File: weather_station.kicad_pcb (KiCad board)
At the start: 2 copper layers, 28 parts, among them J1 Conn_01x10_Pin, J2 Conn_01x04, J3 Conn_01x04, J5 USB_C_Receptacle_USB2.0_16P, J6 JTAG_connector, SW1 SW_Push, U1 USBLC6-2SC6, U2 AZ1117CH2-3.3, U4 STM32F103RGTx, X1 831066657

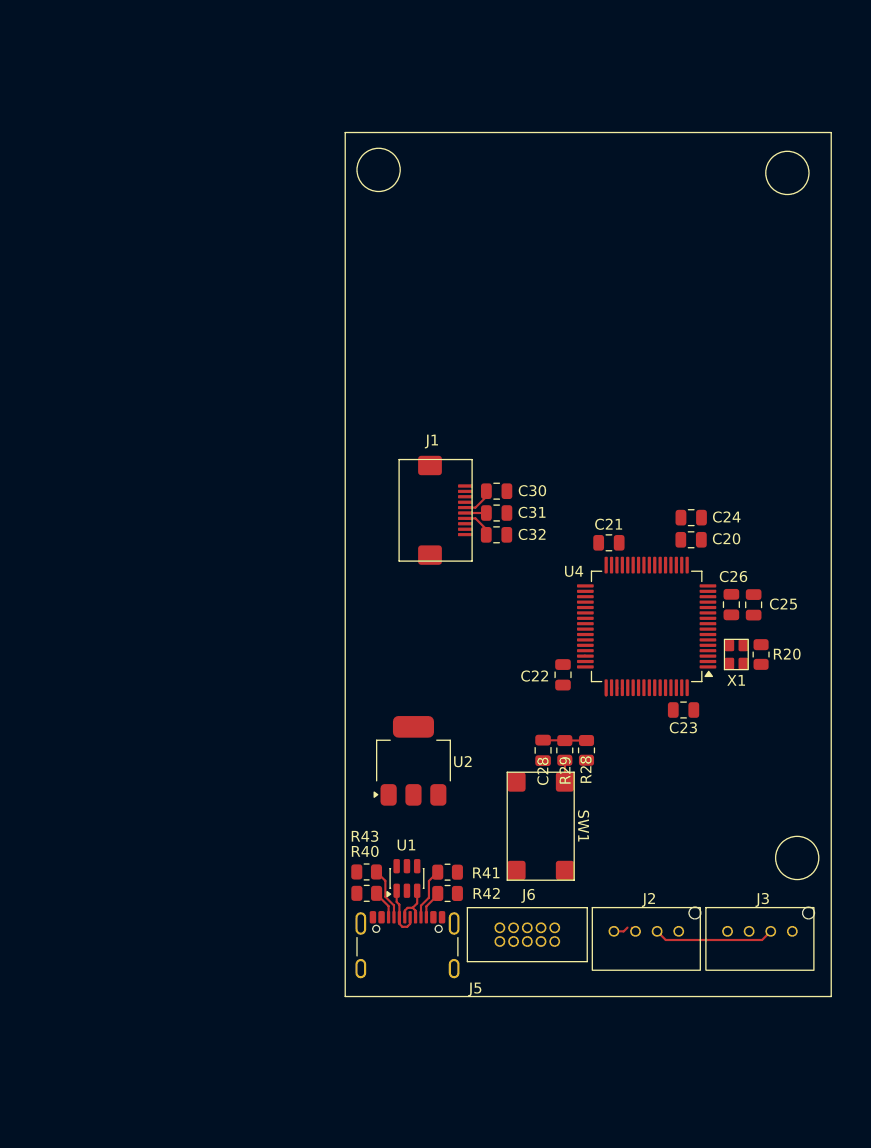
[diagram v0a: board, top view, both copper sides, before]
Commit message: Added planes in routing
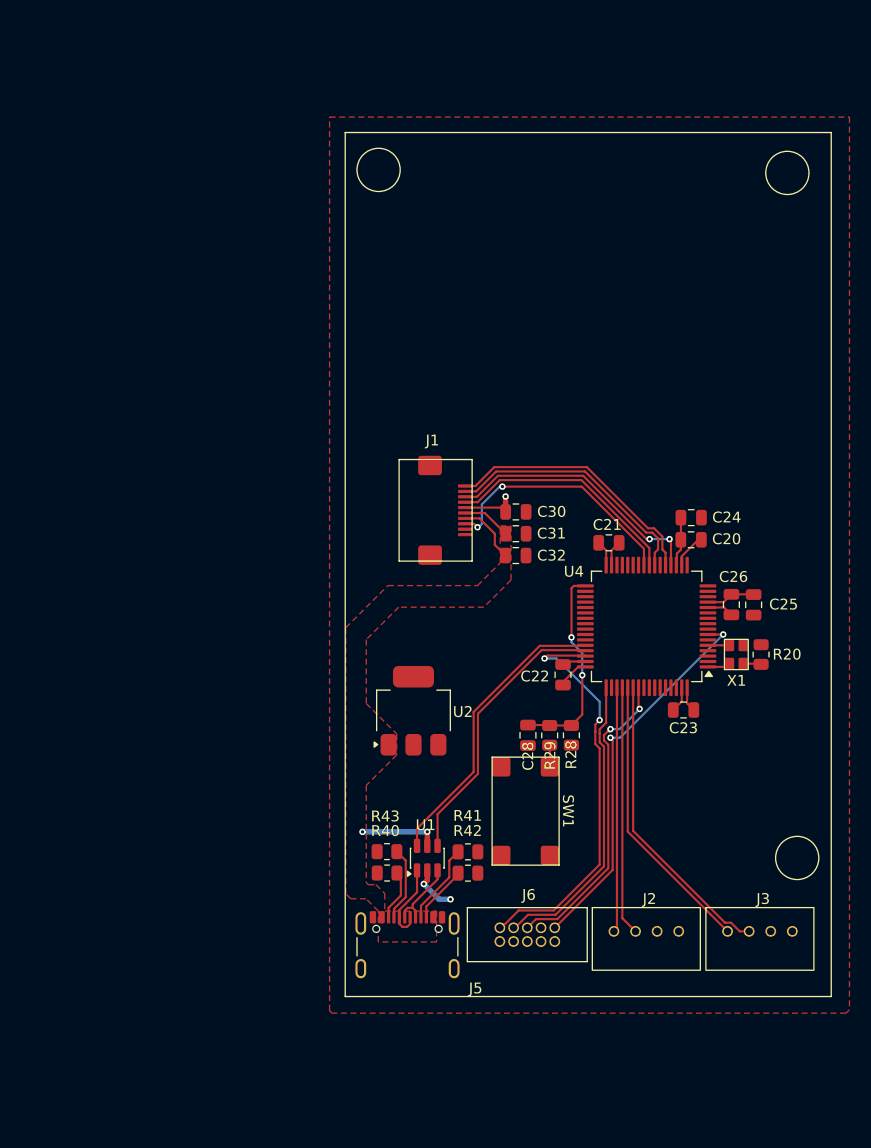
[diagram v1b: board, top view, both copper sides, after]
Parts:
- moved U2 4.64 mm to (96.4, 113.6)
- moved U1 2.66 mm to (97.7, 127.2)
- moved R40 2.66 mm to (93.9, 128.6)
- moved R41 2.66 mm to (101.4, 126.7)
- moved R42 2.66 mm to (101.4, 128.6)
- moved R43 2.66 mm to (93.9, 126.6)
- moved C30 2.62 mm to (105.8, 95.2)
- moved C31 2.62 mm to (105.8, 97.2)
- moved C32 2.62 mm to (105.8, 99.2)
- moved C28 1.98 mm to (107.0, 115.9)
- moved R28 1.98 mm to (111.0, 115.9)
- moved SW1 1.98 mm to (106.8, 122.9)
- moved R29 1.98 mm to (109.0, 115.9)
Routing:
- net /Microcontroller/swdio: track 0.07 -> 37.8 mm, vias 0 -> 2
- net /Microcontroller/reset: track 0.00 -> 35.7 mm, vias 0 -> 2
- net /Microcontroller/swo: track 0.00 -> 28.7 mm, vias 0 -> 2
- net /Connectors/sensor_2_rx: track 0.00 -> 27.8 mm
- net /Connectors/usb_dm: track 0.00 -> 27.5 mm
- net /Microcontroller/swclk: track 0.76 -> 27.7 mm
- net /Connectors/sensor_2_tx: track 0.00 -> 26.4 mm
- net /Connectors/usb_dp: track 0.00 -> 26.2 mm
- net /Display/display_cs: track 0.00 -> 24.6 mm, vias 0 -> 2
- net /Display/display_sclk: track 0.00 -> 24.4 mm
- net /Display/display_mosi: track 0.00 -> 23.8 mm
- net /Display/display_extmode: track 0.00 -> 23.2 mm, vias 0 -> 2
- net /Connectors/sensor_1_rx: track 0.55 -> 23.1 mm
- net /Display/display_extcomin: track 0.00 -> 22.1 mm
- net /Connectors/sensor_1_tx: track 1.47 -> 22.7 mm
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- added copper zone on F.Cu, net +5V
- added copper zone on F.Cu, net GND

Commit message: Created board outline
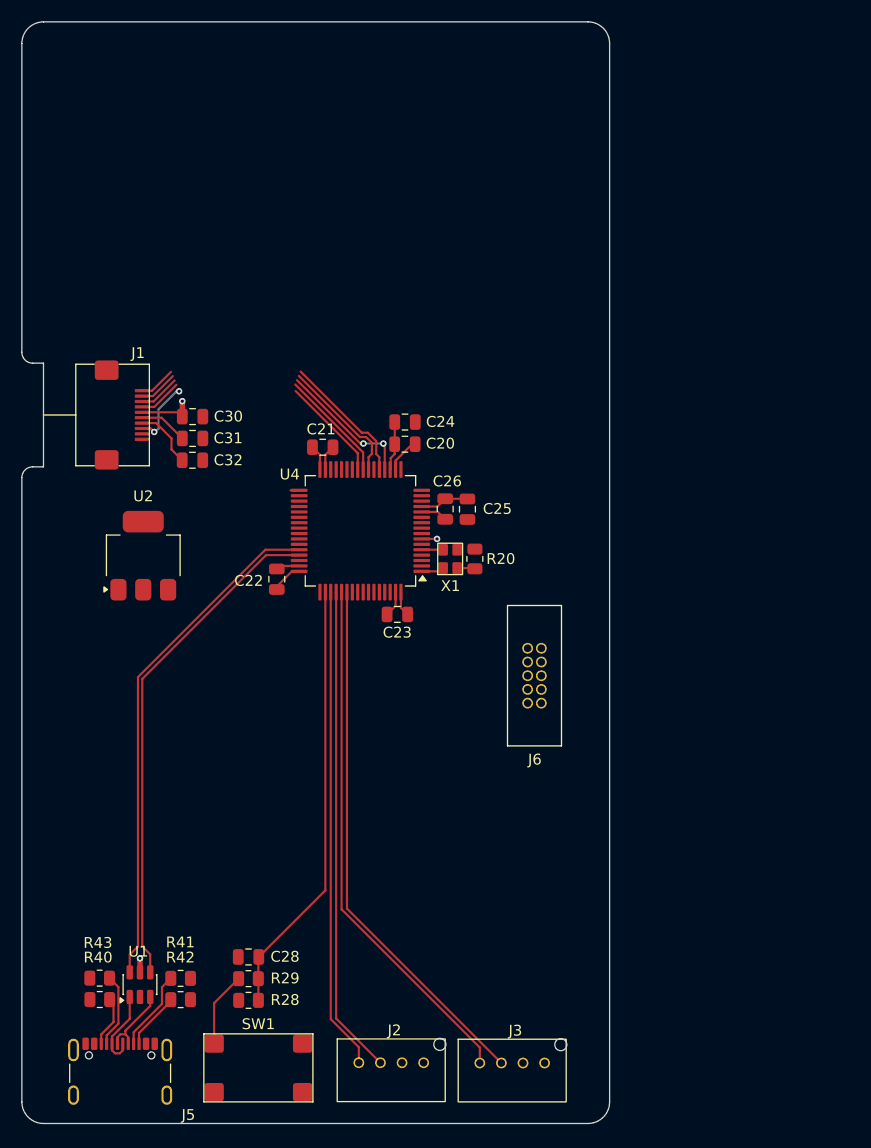
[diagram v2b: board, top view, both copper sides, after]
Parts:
- moved R28 38.7 mm to (81.1, 140.4), turned to 0 degrees
- moved R29 35.8 mm to (81.1, 138.4), turned to 180 degrees
- moved SW1 34.3 mm to (82.0, 146.7), turned to 0 degrees
- moved C28 33.0 mm to (81.1, 136.4), turned to 180 degrees
- moved C32 31.2 mm to (75.9, 90.4)
- moved J1 31.2 mm to (70.6, 86.2)
- moved C30 31.2 mm to (75.9, 86.4)
- moved C31 31.2 mm to (75.9, 88.4)
- moved U1 29.1 mm to (71.0, 139.0)
- moved J5 29.1 mm to (69.2, 148.1)
- moved R40 29.1 mm to (67.3, 140.3)
- moved R41 29.1 mm to (74.8, 138.4)
- moved R42 29.1 mm to (74.8, 140.3)
- moved R43 29.1 mm to (67.3, 138.3)
- moved U2 28.8 mm to (71.3, 99.2)
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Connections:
- C28 pad 1: Net-(U4-PB12) -> Net-(U4-PA15)
- R28 pad 2: Net-(U4-PB12) -> Net-(U4-PA15)
- R29 pad 1: Net-(U4-PB12) -> Net-(U4-PA15)
- U4 pad 33: Net-(U4-PB12) -> unconnected-(U4-PB12-Pad33)
- U4 pad 50: unconnected-(U4-PA15-Pad50) -> Net-(U4-PA15)
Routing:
- net Net-(U4-PA15): track 0.00 -> 40.4 mm
- net /Microcontroller/swdio: track 37.8 -> 0.07 mm, vias 2 -> 0
- net /Microcontroller/reset: track 35.7 -> 1.42 mm, vias 2 -> 1
- net /Microcontroller/swo: track 28.7 -> 0.00 mm, vias 2 -> 0
- net /Microcontroller/swclk: track 27.7 -> 0.00 mm
- net /Connectors/sensor_2_tx: track 26.4 -> 48.9 mm
- net /Connectors/sensor_1_rx: track 23.1 -> 45.3 mm
- net /Connectors/sensor_1_tx: track 22.7 -> 44.7 mm
- net /Connectors/sensor_2_rx: track 27.8 -> 49.5 mm
- net /Connectors/usb_dp: track 26.2 -> 46.8 mm
- net /Connectors/usb_dm: track 27.5 -> 47.5 mm
- net Net-(U4-PB12): track 18.9 -> 0.00 mm, vias 2 -> 0
- net /Display/display_sclk: track 24.4 -> 15.9 mm
- net /Display/display_mosi: track 23.8 -> 15.6 mm
- net /Display/display_cs: track 24.6 -> 16.7 mm
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- removed copper zone on F.Cu, net +5V
- removed copper zone on F.Cu, net GND
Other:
- board outline added: 54.4 x 102 mm
